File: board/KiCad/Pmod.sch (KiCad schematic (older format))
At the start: 1 part

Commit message: First pmod side wiring
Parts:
- removed P?: CONN_02X06, symbol CONN_02X06
- added P1, P2: PMOD_2x6, pmod:Pmod, symbol PMOD_2x6
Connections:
- net labels added: PIO0, PIO1, PIO10, PIO11, PIO12, PIO13, PIO14, PIO15, PIO2, PIO3, PIO4, PIO5, PIO6, PIO7, PIO8, PIO9
- net labels removed: pmod0, pmod1, pmod2, pmod3, pmod4, pmod5, pmod6, pmod7
- wire segments 16 -> 53
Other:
- note added: "This is the board connector"
- note added: "This is the extra breakout"

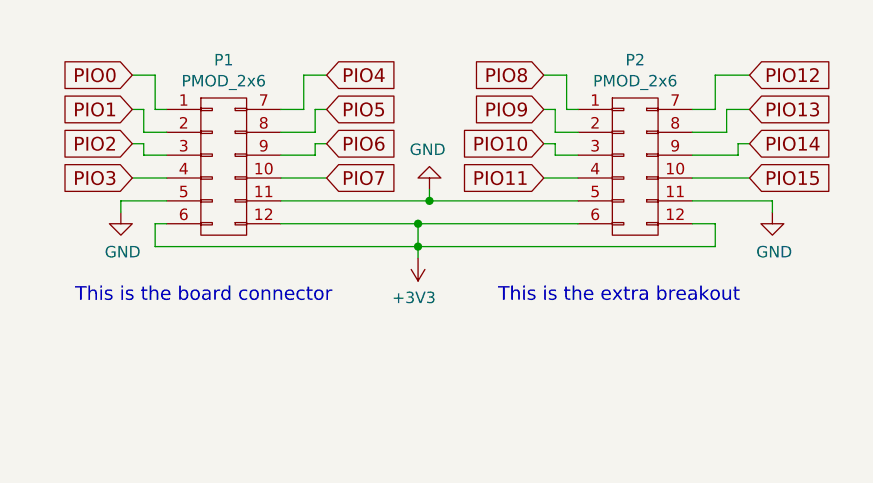
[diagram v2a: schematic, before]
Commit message: 1.2V power supply
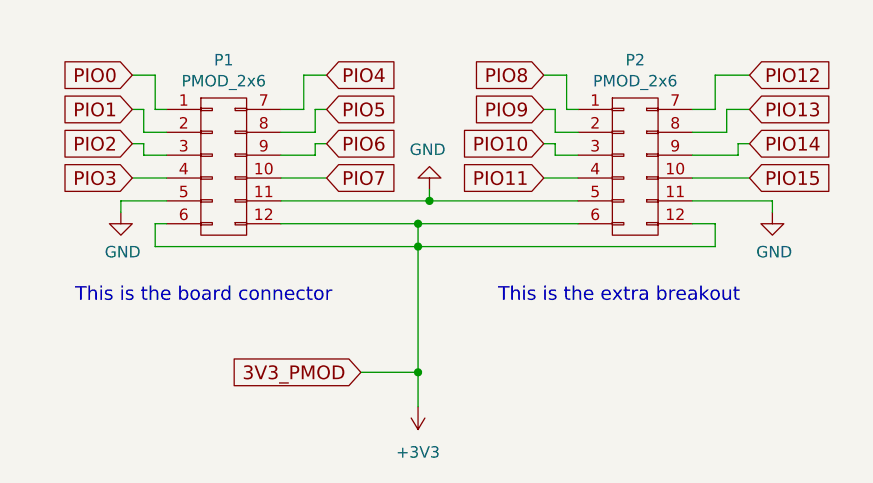
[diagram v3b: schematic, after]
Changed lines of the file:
@@
 EESchema Schematic File Version 2
+LIBS:LMS6002-Pmod-rescue
 LIBS:power
 LIBS:device
@@
 $Descr A4 11693 8268
 encoding utf-8
-Sheet 2 4
+Sheet 2 5
 Title ""
 Date ""
@@
 This is the extra breakout
 $Comp
-L +3V3 #PWR3
+L +3V3 #PWR2
 U 1 1 56A608EC
-P 5850 4150
-F 0 "#PWR3" H 5850 4000 50  0001 C CNN
-F 1 "+3V3" H 5868 4324 50  0000 C CNN
-F 2 "" H 5850 4150 50  0000 C CNN
-F 3 "" H 5850 4150 50  0000 C CNN
-	1    5850 4150
+P 5850 4800
+F 0 "#PWR2" H 5850 4650 50  0001 C CNN
+F 1 "+3V3" H 5850 5000 50  0000 C CNN
+F 2 "" H 5850 4800 50  0000 C CNN
+F 3 "" H 5850 4800 50  0000 C CNN
+	1    5850 4800
 	-1   0    0    1
 $EndComp
@@
 	5250 3900 6550 3900
 $Comp
-L GND #PWR4
+L GND #PWR3
 U 1 1 56A609AB
 P 5900 3850
-F 0 "#PWR4" H 5900 3600 50  0001 C CNN
+F 0 "#PWR3" H 5900 3600 50  0001 C CNN
 F 1 "GND" H 5908 3676 50  0000 C CNN
 F 2 "" H 5900 3850 50  0000 C CNN
@@
 $EndComp
 Wire Wire Line
-	5850 4000 5850 4150
+	5850 4000 5850 4800
 Connection ~ 5850 4000
 Wire Wire Line
@@
 Connection ~ 5900 3900
 $Comp
-L GND #PWR5
+L GND #PWR4
 U 1 1 56A60AD2
 P 7400 3950
-F 0 "#PWR5" H 7400 3700 50  0001 C CNN
+F 0 "#PWR4" H 7400 3700 50  0001 C CNN
 F 1 "GND" H 7408 3776 50  0000 C CNN
 F 2 "" H 7400 3950 50  0000 C CNN
@@
 	4550 3900 4550 3950
 $Comp
-L GND #PWR2
+L GND #PWR1
 U 1 1 56A60B36
 P 4550 3950
-F 0 "#PWR2" H 4550 3700 50  0001 C CNN
+F 0 "#PWR1" H 4550 3700 50  0001 C CNN
 F 1 "GND" H 4558 3776 50  0000 C CNN
 F 2 "" H 4550 3950 50  0000 C CNN
@@
 Wire Wire Line
 	6400 3800 6550 3800
+Text GLabel 5600 4650 0    60   Input ~ 0
+3V3_PMOD
+Wire Wire Line
+	5600 4650 5850 4650
+Connection ~ 5850 4650
 $EndSCHEMATC

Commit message: minor changes
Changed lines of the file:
@@
 	5600 4650 5850 4650
 Connection ~ 5850 4650
+Wire Notes Line
+	4100 3100 5800 3100
+Wire Notes Line
+	5800 3100 5800 4400
+Wire Notes Line
+	5800 4400 4100 4400
+Wire Notes Line
+	4100 4400 4100 3100
+Wire Notes Line
+	6000 3100 7700 3100
+Wire Notes Line
+	7700 3100 7700 4400
+Wire Notes Line
+	7700 4400 6000 4400
+Wire Notes Line
+	6000 4400 6000 3100
 $EndSCHEMATC
